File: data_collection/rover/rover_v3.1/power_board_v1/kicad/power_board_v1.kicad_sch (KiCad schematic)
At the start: 96 parts, among them J1 XT60_BATT, J10 from Pi USB2, J11 UPDI prog (UPDI/3V3/GND), J12 XT30 fallback pads, J2 PANEL_SW, J3 USB-C PWR OUT (TH shell), J4 USB_A radio1, J5 USB_A radio2, J6 AUX 5V 2A, J7 PI GPIO harness, J8 AUX_CTL out (JST-GH), J9 from Pi USB1, Q2 CSD18543Q3A diode, Q3 CSD18543Q3A switch, U1 LM5145 5.1V rail A, U2 LM5145 5.1V rail B, U3 ATtiny816 (VQFN), U4 LM74800-Q1, U5 INA226 (addr 0x40), U6 TPS7A1633 3V3 60V LDO, U7 TPS2553 1.7A, U8 TPS2553 1.7A, U9 AP2112K-3.3 (switched)

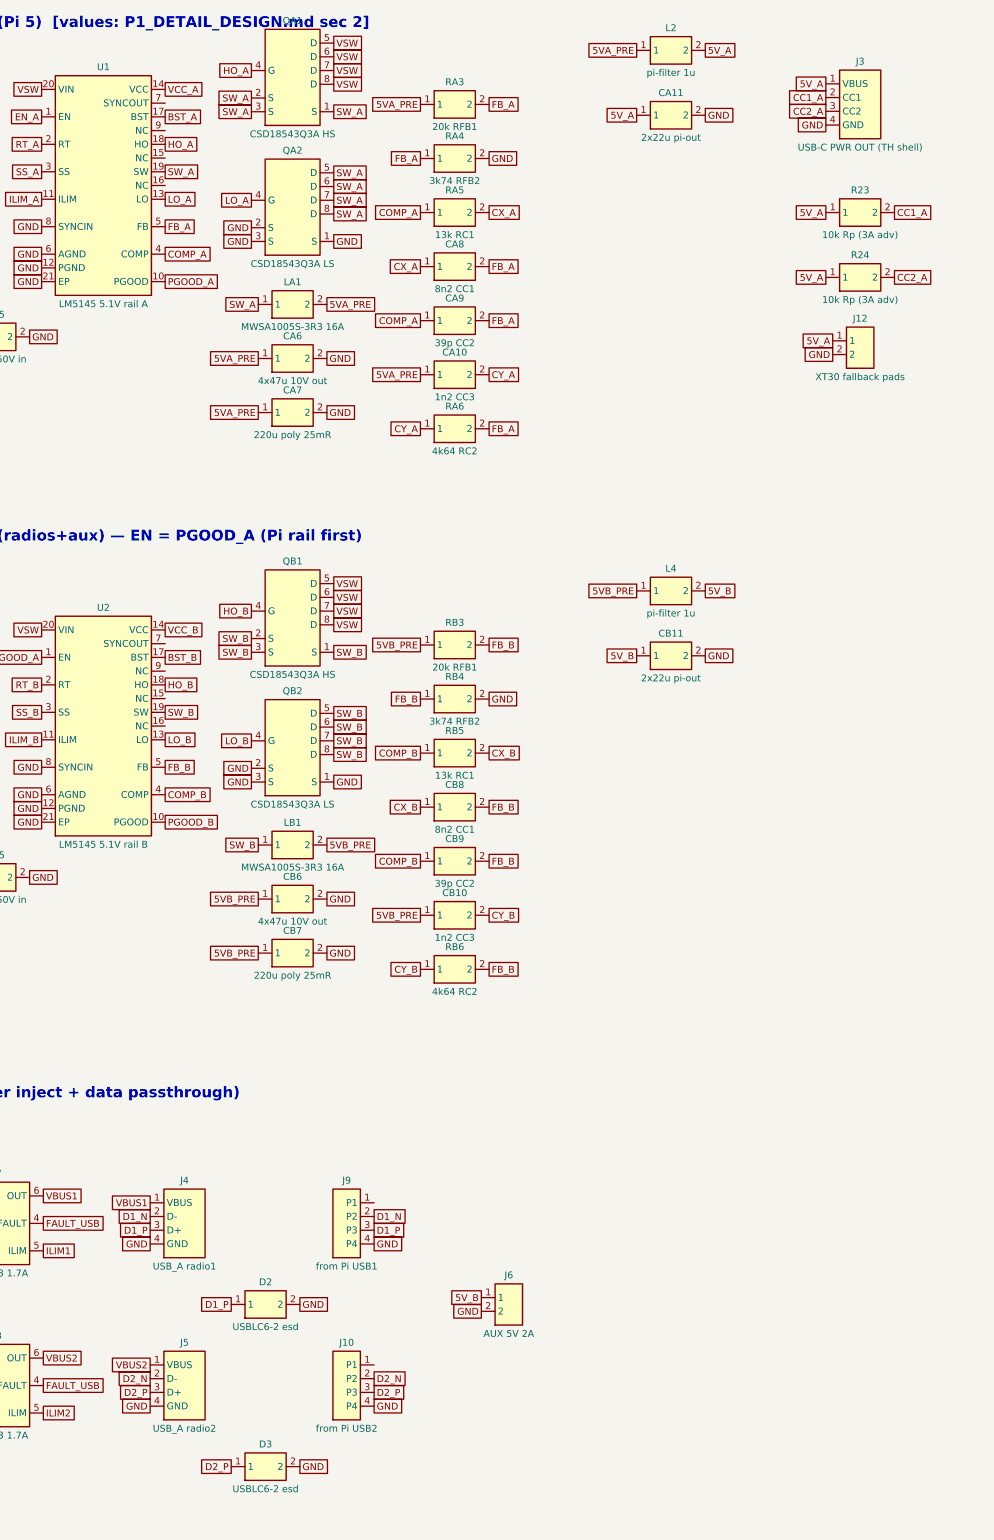
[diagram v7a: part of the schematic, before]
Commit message: P3 footprints: all 96 components assigned (netlist-verified); custom VQFN-20 LM5145RGY + WSON-12 LM74800DRR footprints authored from TI drawings, pcbnew-validated; USB-C symbol on real GCT USB4105 pads; fp-lib-table; docs synced
Co-Authored-By: Claude Fable 5 <noreply@anthropic.com>
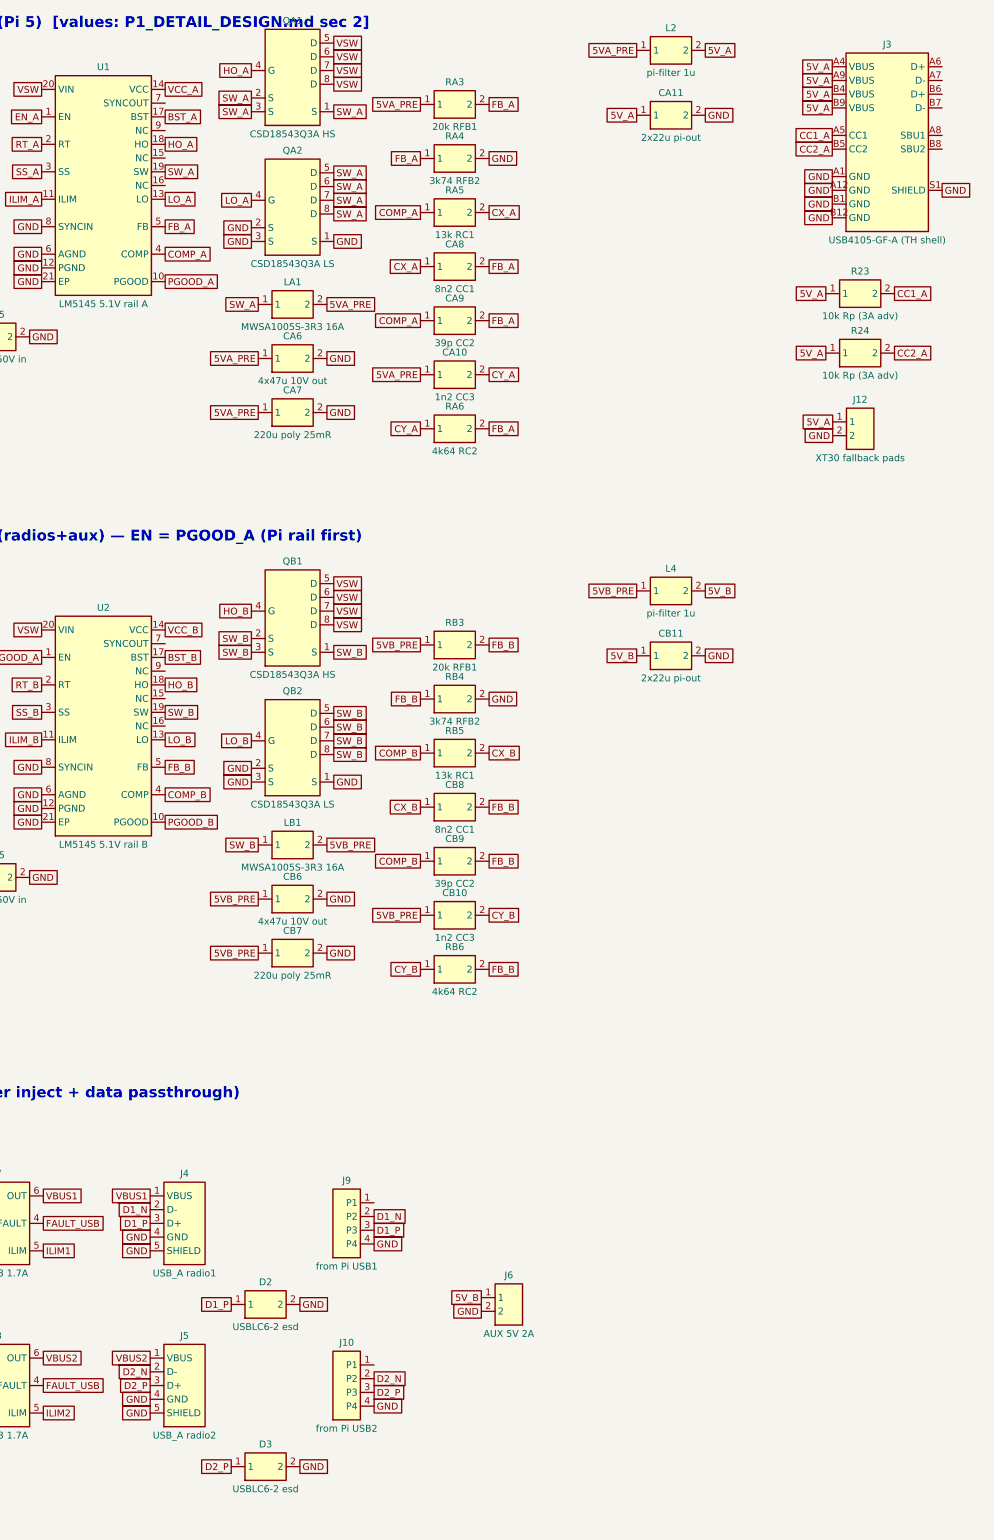
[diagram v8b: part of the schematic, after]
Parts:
- C1, C2, C3, C4, CA1, CA10, CA3, CA4, CA8, CA9, CB1, CB10, CB3, CB4, CB8, CB9: footprint (none) -> Capacitor_SMD:C_0402_1005Metric
- CA11, CB11: footprint (none) -> Capacitor_SMD:C_1206_3216Metric
- CA2, CB2: footprint (none) -> Capacitor_SMD:C_0603_1608Metric
- CA5, CA6, CB5, CB6: footprint (none) -> Capacitor_SMD:C_1210_3225Metric
- CA7, CB7: footprint (none) -> Capacitor_SMD:CP_Elec_6.3x5.9
- D1: footprint (none) -> Diode_SMD:D_SMB
- D2, D3, U7, U8: footprint (none) -> Package_TO_SOT_SMD:SOT-23-6
- D4: footprint (none) -> LED_SMD:LED_0805_2012Metric
- F1: footprint (none) -> Fuse:FuseHolder_Blade_ATO_Littelfuse_FLR_178.6165
- J1: footprint (none) -> Connector_AMASS:AMASS_XT60PW-M_1x02_P7.20mm_Horizontal
- J10, J9: footprint (none) -> Connector_PinHeader_2.54mm:PinHeader_1x04_P2.54mm_Vertical
- J11: footprint (none) -> Connector_JST:JST_GH_BM03B-GHS-TBT_1x03-1MP_P1.25mm_Vertical
- J12: footprint (none) -> Connector_AMASS:AMASS_XT30PW-M_1x02_P2.50mm_Horizontal
- J2, J8: footprint (none) -> Connector_JST:JST_GH_BM02B-GHS-TBT_1x02-1MP_P1.25mm_Vertical
- J3: value USB-C PWR OUT (TH shell) -> USB4105-GF-A (TH shell); footprint (none) -> Connector_USB:USB_C_Receptacle_GCT_USB4105-xx-A_16P_TopMnt_Horizontal
- J4, J5: footprint (none) -> Connector_USB:USB_A_CNCTech_1001-011-01101_Horizontal
- J6: footprint (none) -> TerminalBlock_Phoenix:TerminalBlock_Phoenix_MKDS-1,5-2_1x02_P5.00mm_Horizontal
- J7: footprint (none) -> Connector_JST:JST_GH_SM08B-GHS-TB_1x08-1MP_P1.25mm_Horizontal
- L2, L4: footprint (none) -> Inductor_SMD:L_Chilisin_BMRx00060630
- LA1, LB1: footprint (none) -> Inductor_SMD:L_Sunlord_MWSA1005S
- Q2, Q3, QA1, QA2, QB1, QB2: footprint (none) -> Package_SON:VSON-8_3.3x3.3mm_P0.65mm_NexFET
- R1, R10, R11, R16, R17, R18, R19, R2, R21, R22, R23, R24, R25, R26, R27, R28, R29, R3, R30, R4, R5, RA1, RA2, RA3, RA4, RA5, RA6, RB1, RB2, RB3, RB4, RB5, RB6: footprint (none) -> Resistor_SMD:R_0402_1005Metric
- R20: footprint (none) -> Resistor_SMD:R_2512_6332Metric
- U1, U2: footprint (none) -> power_board_v1:VQFN-20_3.5x4.5_P0.5_LM5145RGY
- U3: footprint (none) -> Package_DFN_QFN:QFN-20-1EP_3x3mm_P0.4mm_EP1.65x1.65mm
- U4: footprint (none) -> power_board_v1:WSON-12_3x3_P0.5_LM74800DRR
- U5: footprint (none) -> Package_SO:VSSOP-10_3x3mm_P0.5mm
- U6: footprint (none) -> Package_SO:MSOP-8-1EP_3x3mm_P0.65mm_EP1.68x1.88mm
- U9: footprint (none) -> Package_TO_SOT_SMD:SOT-23-5
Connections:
- net 5V_A: now also J3.A4 (VBUS), J3.A9 (VBUS), J3.B4 (VBUS), J3.B9 (VBUS); no longer J3.1 (VBUS)
- net CC1_A: now also J3.A5 (CC1); no longer J3.2 (CC1)
- net CC2_A: now also J3.B5 (CC2); no longer J3.3 (CC2)
- net GND: now also J3.A1 (GND), J3.A12 (GND), J3.B1 (GND), J3.B12 (GND), J3.S1 (SHIELD), J4.5 (SHIELD), J5.5 (SHIELD); no longer J3.4 (GND)
